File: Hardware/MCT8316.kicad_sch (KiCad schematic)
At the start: 17 parts, among them J5 Screw_Terminal_01x03, U11 PC817

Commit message: Update Sche
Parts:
- removed R31: 10K, IVS_FOOTPRINTS:R_0603, symbol IVS_SYMBOLS:R
- removed U11: PC817, Package_DIP:DIP-4_W7.62mm, symbol Isolator:PC817
- added C22: 1uF, IVS_FOOTPRINTS:C_0603, symbol IVS_SYMBOLS:C
- added J6: Screw_Terminal_01x03, TerminalBlock:TerminalBlock_bornier-3_P5.08mm, symbol Connector:Screw_Terminal_01x03
- added J7, J8: Conn_01x03_Pin, Connector_PinHeader_2.54mm:PinHeader_1x03_P2.54mm_Vertical, symbol IVS_SYMBOLS:Conn_01x03_Pin
- added JP1, JP2: SolderJumper_2_Open, IVS_FOOTPRINTS:SolderJumper-2_P1.3mm_Open_RoundedPad1.0x1.5mm, symbol IVS_SYMBOLS:SolderJumper_2_Open
- added L2: 47uH, Inductor_SMD:L_1812_4532Metric, symbol Device:L
- added R32: 330R, IVS_FOOTPRINTS:R_0603, symbol IVS_SYMBOLS:R
- added R33: 1K, IVS_FOOTPRINTS:R_0603, symbol IVS_SYMBOLS:R
- added U12: ISO7721DR, IVS_FOOTPRINTS:SOIC-8, symbol IVS_SYMBOLS:ISO7721DR
- added U13, U14, U15: EL817, Package_DIP:DIP-4_W7.62mm, symbol IVS_SYMBOLS:EL817
- J5: footprint (none) -> TerminalBlock:TerminalBlock_bornier-3_P5.08mm
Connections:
- net +5V_CS: now also U12.8 (VCC2)
- net AVDD: now also J8.3 (Pin_3)
- net GNDD: now also U12.5 (GND2), U13.2, U14.2, U15.2
- net MCT_DIR: now also U15.1
- net MCT_FAULT: now also U13.1
- net MCT_FG: now also R32.2
- net MCT_SCL: now also J6.1 (Pin_1), J6.2 (Pin_2), JP1.2 (B), JP2.2 (B)
- net PWM_BLDC: now also U12.6 (OUTB)
- net MCT_DRBOFF: now reaches U10.21 (DRVOFF)
- net BUCK: now reaches U10.3 (FB_BK)
- net BUCK: now also C22.2, J7.3 (Pin_3), L2.2
- net MCT_BRAKE: now reaches U10.35 (BRAKE)
- net MCT_BRAKE: now also U14.1
- net at U10.4 (GND_BK): now also C22.1
- net at U10.5 (SW_BK): now also L2.1
- net at R25.2: now also U12.3 (INB)
- new net: R32.1, U12.7 (INA)
- new net +3V3: J8.1 (Pin_1)
- new net +3V3_MCU: J8.2 (Pin_2)
- new net +5V: J7.1 (Pin_1), R33.1, U12.1 (VCC1)
- new net +5VA: J7.2 (Pin_2)
- new net GND: J6.3 (Pin_3), U12.4 (GND1), U13.3, U14.3, U15.3
- new net MCU_BRAKE: U14.4
- new net MCU_DIR: U15.4
- new net MCU_FAULT: U13.4
- new net MCU_FG: R33.2, U12.2 (OUTA)
- new net MCU_SCL: JP2.1 (A)
- new net MCU_SDA: JP1.1 (A)
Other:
- moved on the sheet: C20, C21, F1

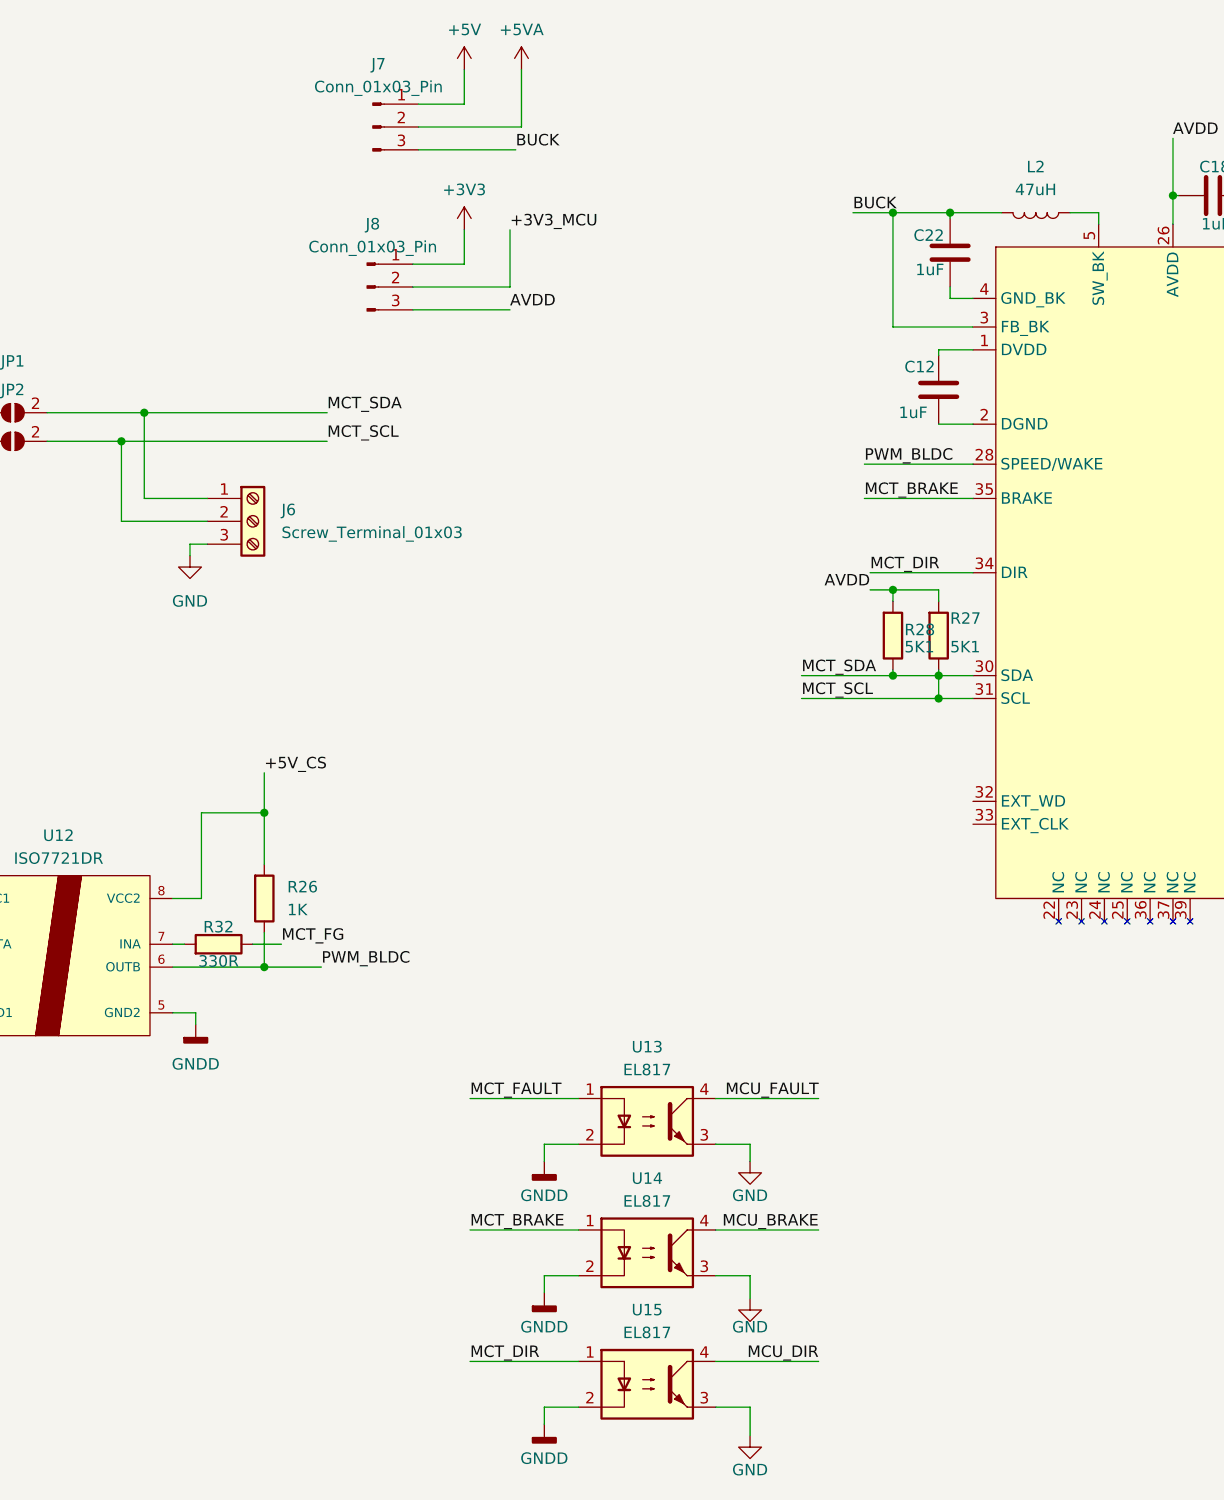
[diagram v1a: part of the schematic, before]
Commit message: Hie BTS, fix GND opto MCT
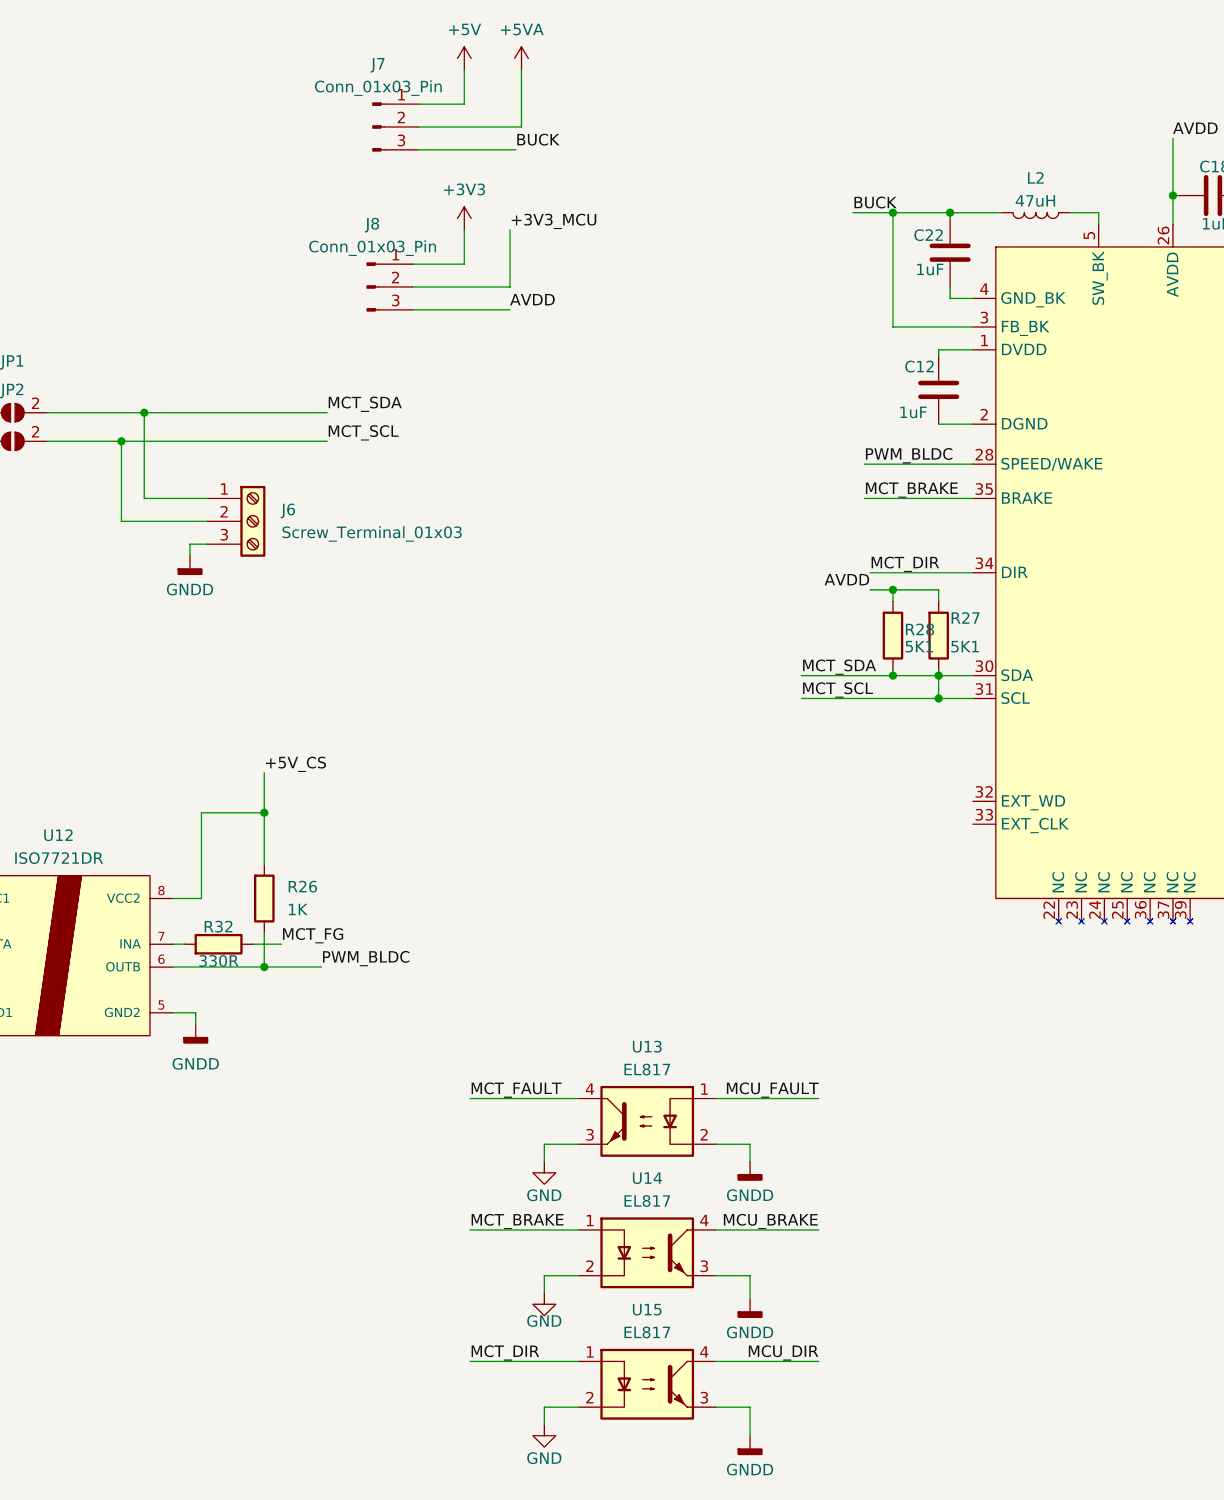
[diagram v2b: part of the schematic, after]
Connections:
- net GND: now also U14.2, U15.2; no longer J6.3 (Pin_3), U14.3, U15.3
- net GNDD: now also J6.3 (Pin_3), U14.3, U15.3; no longer U14.2, U15.2
- net MCT_FAULT: now also U13.4; no longer U13.1
- net MCU_FAULT: now also U13.1; no longer U13.4
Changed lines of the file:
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@@
     (effects (font (size 1.27 1.27)) (justify left bottom))
   )
-  (symbol (lib_id "power:GND") (at 151.13 162.56 0) (unit 1)
-    (in_bom yes) (on_board yes) (dnp no)
-    (property "Reference" "#PWR033" (at 151.13 168.91 0)
-      (effects (font (size 1.27 1.27)) hide)
-    )
-    (property "Value" "GND" (at 151.13 165.735 0)
-      (effects (font (size 1.27 1.27)))
-    )
-    (property "Footprint" "" (at 151.13 162.56 0)
-      (effects (font (size 1.27 1.27)) hide)
-    )
-    (property "Datasheet" "" (at 151.13 162.56 0)
+  (symbol (lib_id "power:GND") (at 128.27 161.925 0) (unit 1)
+    (in_bom yes) (on_board yes) (dnp no)
+    (property "Reference" "#PWR033" (at 128.27 168.275 0)
+      (effects (font (size 1.27 1.27)) hide)
+    )
+    (property "Value" "GND" (at 128.27 165.1 0)
+      (effects (font (size 1.27 1.27)))
+    )
+    (property "Footprint" "" (at 128.27 161.925 0)
+      (effects (font (size 1.27 1.27)) hide)
+    )
+    (property "Datasheet" "" (at 128.27 161.925 0)
       (effects (font (size 1.27 1.27)) hide)
     )
@@
     )
   )
+  (symbol (lib_id "power:GNDD") (at 88.9 80.01 0) (unit 1)
+    (in_bom yes) (on_board yes) (dnp no) (fields_autoplaced)
+    (property "Reference" "#PWR06" (at 88.9 86.36 0)
+      (effects (font (size 1.27 1.27)) hide)
+    )
+    (property "Value" "GNDD" (at 88.9 83.82 0)
+      (effects (font (size 1.27 1.27)))
+    )
+    (property "Footprint" "" (at 88.9 80.01 0)
+      (effects (font (size 1.27 1.27)) hide)
+    )
+    (property "Datasheet" "" (at 88.9 80.01 0)
+      (effects (font (size 1.27 1.27)) hide)
+    )
+    (pin "1")
+    (instances
+      (project "DriverMotor"
+        (path "/8a82bd86-ff43-47ee-a4c0-46ff08914251/719245fa-8c27-4cf8-8d61-6f38548a0446"
+          (reference "#PWR06") (unit 1)
+        )
+      )
+    )
+  )
   (symbol (lib_id "IVS_SYMBOLS:EL817") (at 139.7 157.48 0) (unit 1)
     (in_bom yes) (on_board yes) (dnp no) (fields_autoplaced)
@@
     )
   )
-  (symbol (lib_id "power:GNDD") (at 128.27 147.32 0) (unit 1)
-    (in_bom yes) (on_board yes) (dnp no) (fields_autoplaced)
-    (property "Reference" "#PWR03" (at 128.27 153.67 0)
-      (effects (font (size 1.27 1.27)) hide)
-    )
-    (property "Value" "GNDD" (at 128.27 151.13 0)
-      (effects (font (size 1.27 1.27)))
-    )
-    (property "Footprint" "" (at 128.27 147.32 0)
-      (effects (font (size 1.27 1.27)) hide)
-    )
-    (property "Datasheet" "" (at 128.27 147.32 0)
+  (symbol (lib_id "power:GNDD") (at 151.13 147.32 0) (unit 1)
+    (in_bom yes) (on_board yes) (dnp no) (fields_autoplaced)
+    (property "Reference" "#PWR03" (at 151.13 153.67 0)
+      (effects (font (size 1.27 1.27)) hide)
+    )
+    (property "Value" "GNDD" (at 151.13 151.13 0)
+      (effects (font (size 1.27 1.27)))
+    )
+    (property "Footprint" "" (at 151.13 147.32 0)
+      (effects (font (size 1.27 1.27)) hide)
+    )
+    (property "Datasheet" "" (at 151.13 147.32 0)
       (effects (font (size 1.27 1.27)) hide)
     )
@@
     )
   )
-  (symbol (lib_id "power:GNDD") (at 128.27 176.53 0) (unit 1)
-    (in_bom yes) (on_board yes) (dnp no) (fields_autoplaced)
-    (property "Reference" "#PWR010" (at 128.27 182.88 0)
-      (effects (font (size 1.27 1.27)) hide)
-    )
-    (property "Value" "GNDD" (at 128.27 180.34 0)
-      (effects (font (size 1.27 1.27)))
-    )
-    (property "Footprint" "" (at 128.27 176.53 0)
-      (effects (font (size 1.27 1.27)) hide)
-    )
-    (property "Datasheet" "" (at 128.27 176.53 0)
+  (symbol (lib_id "power:GNDD") (at 151.13 177.8 0) (unit 1)
+    (in_bom yes) (on_board yes) (dnp no)
+    (property "Reference" "#PWR010" (at 151.13 184.15 0)
+      (effects (font (size 1.27 1.27)) hide)
+    )
+    (property "Value" "GNDD" (at 151.13 181.61 0)
+      (effects (font (size 1.27 1.27)))
+    )
+    (property "Footprint" "" (at 151.13 177.8 0)
+      (effects (font (size 1.27 1.27)) hide)
+    )
+    (property "Datasheet" "" (at 151.13 177.8 0)
       (effects (font (size 1.27 1.27)) hide)
     )
@@
   (symbol (lib_id "Device:L") (at 182.88 41.91 270) (unit 1)
     (in_bom yes) (on_board yes) (dnp no) (fields_autoplaced)
-    (property "Reference" "L2" (at 182.88 36.83 90)
-      (effects (font (size 1.27 1.27)))
-    )
-    (property "Value" "47uH" (at 182.88 39.37 90)
+    (property "Reference" "L2" (at 182.88 38.1 90)
+      (effects (font (size 1.27 1.27)))
+    )
+    (property "Value" "47uH" (at 182.88 40.64 90)
       (effects (font (size 1.27 1.27)))
     )
@@
     )
   )
-  (symbol (lib_id "power:GND") (at 151.13 177.8 0) (unit 1)
-    (in_bom yes) (on_board yes) (dnp no)
-    (property "Reference" "#PWR048" (at 151.13 184.15 0)
-      (effects (font (size 1.27 1.27)) hide)
-    )
-    (property "Value" "GND" (at 151.13 181.61 0)
-      (effects (font (size 1.27 1.27)))
-    )
-    (property "Footprint" "" (at 151.13 177.8 0)
-      (effects (font (size 1.27 1.27)) hide)
-    )
-    (property "Datasheet" "" (at 151.13 177.8 0)
+  (symbol (lib_id "power:GND") (at 128.27 176.53 0) (unit 1)
+    (in_bom yes) (on_board yes) (dnp no)
+    (property "Reference" "#PWR048" (at 128.27 182.88 0)
+      (effects (font (size 1.27 1.27)) hide)
+    )
+    (property "Value" "GND" (at 128.27 180.34 0)
+      (effects (font (size 1.27 1.27)))
+    )
+    (property "Footprint" "" (at 128.27 176.53 0)
+      (effects (font (size 1.27 1.27)) hide)
+    )
+    (property "Datasheet" "" (at 128.27 176.53 0)
       (effects (font (size 1.27 1.27)) hide)
     )
@@
     )
   )
-  (symbol (lib_id "power:GND") (at 88.9 80.01 0) (unit 1)
-    (in_bom yes) (on_board yes) (dnp no) (fields_autoplaced)
-    (property "Reference" "#PWR031" (at 88.9 86.36 0)
-      (effects (font (size 1.27 1.27)) hide)
-    )
-    (property "Value" "GND" (at 88.9 85.09 0)
-      (effects (font (size 1.27 1.27)))
-    )
-    (property "Footprint" "" (at 88.9 80.01 0)
-      (effects (font (size 1.27 1.27)) hide)
-    )
-    (property "Datasheet" "" (at 88.9 80.01 0)
-      (effects (font (size 1.27 1.27)) hide)
-    )
-    (pin "1")
-    (instances
-      (project "DriverMotor"
-        (path "/8a82bd86-ff43-47ee-a4c0-46ff08914251/719245fa-8c27-4cf8-8d61-6f38548a0446"
-          (reference "#PWR031") (unit 1)
-        )
-      )
-    )
-  )
   (symbol (lib_id "IVS_SYMBOLS:Conn_01x03_Pin") (at 108.585 50.165 0) (unit 1)
     (in_bom yes) (on_board yes) (dnp no) (fields_autoplaced)
@@
     )
   )
-  (symbol (lib_id "power:GNDD") (at 128.27 161.925 0) (unit 1)
-    (in_bom yes) (on_board yes) (dnp no) (fields_autoplaced)
-    (property "Reference" "#PWR08" (at 128.27 168.275 0)
-      (effects (font (size 1.27 1.27)) hide)
-    )
-    (property "Value" "GNDD" (at 128.27 165.735 0)
-      (effects (font (size 1.27 1.27)))
-    )
-    (property "Footprint" "" (at 128.27 161.925 0)
-      (effects (font (size 1.27 1.27)) hide)
-    )
-    (property "Datasheet" "" (at 128.27 161.925 0)
+  (symbol (lib_id "power:GNDD") (at 151.13 162.56 0) (unit 1)
+    (in_bom yes) (on_board yes) (dnp no)
+    (property "Reference" "#PWR08" (at 151.13 168.91 0)
+      (effects (font (size 1.27 1.27)) hide)
+    )
+    (property "Value" "GNDD" (at 151.13 166.37 0)
+      (effects (font (size 1.27 1.27)))
+    )
+    (property "Footprint" "" (at 151.13 162.56 0)
+      (effects (font (size 1.27 1.27)) hide)
+    )
+    (property "Datasheet" "" (at 151.13 162.56 0)
       (effects (font (size 1.27 1.27)) hide)
     )
@@
     )
   )
-  (symbol (lib_id "power:GND") (at 151.13 147.32 0) (unit 1)
-    (in_bom yes) (on_board yes) (dnp no)
-    (property "Reference" "#PWR015" (at 151.13 153.67 0)
-      (effects (font (size 1.27 1.27)) hide)
-    )
-    (property "Value" "GND" (at 151.13 151.13 0)
-      (effects (font (size 1.27 1.27)))
-    )
-    (property "Footprint" "" (at 151.13 147.32 0)
-      (effects (font (size 1.27 1.27)) hide)
-    )
-    (property "Datasheet" "" (at 151.13 147.32 0)
+  (symbol (lib_id "power:GND") (at 128.27 147.32 0) (unit 1)
+    (in_bom yes) (on_board yes) (dnp no)
+    (property "Reference" "#PWR015" (at 128.27 153.67 0)
+      (effects (font (size 1.27 1.27)) hide)
+    )
+    (property "Value" "GND" (at 128.27 151.13 0)
+      (effects (font (size 1.27 1.27)))
+    )
+    (property "Footprint" "" (at 128.27 147.32 0)
+      (effects (font (size 1.27 1.27)) hide)
+    )
+    (property "Datasheet" "" (at 128.27 147.32 0)
       (effects (font (size 1.27 1.27)) hide)
     )
@@
     )
   )
-  (symbol (lib_id "IVS_SYMBOLS:EL817") (at 139.7 142.875 0) (unit 1)
-    (in_bom yes) (on_board yes) (dnp no) (fields_autoplaced)
+  (symbol (lib_id "IVS_SYMBOLS:EL817") (at 139.7 142.875 0) (mirror y) (unit 1)
+    (in_bom yes) (on_board yes) (dnp no)
     (property "Reference" "U13" (at 139.7 134.62 0)
       (effects (font (size 1.27 1.27)))
@@
       (effects (font (size 1.27 1.27)))
     )
-    (property "Footprint" "Package_DIP:DIP-4_W7.62mm" (at 134.62 147.955 0)
+    (property "Footprint" "Package_DIP:DIP-4_W7.62mm" (at 144.78 147.955 0)
       (effects (font (size 1.27 1.27) italic) (justify left) hide)
     )

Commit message: Up schematic
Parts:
- removed U10: ~, symbol IVS_SYMBOLS:MxT-F8316
- added J12: Screw_Terminal_01x04, Connector_PinHeader_2.54mm:PinHeader_1x04_P2.54mm_Vertical, symbol Connector:Screw_Terminal_01x04
- added R35: 1K, IVS_FOOTPRINTS:R_0603, symbol IVS_SYMBOLS:R
- added U10: MCT8316, IVS_FOOTPRINTS:VQFN-40-1EP_7x7mm_P0.5mm_EP5.7x3.7mm_ThermalVias, symbol IVS_SYMBOLS:MCT8316
- C21: footprint Capacitor_THT:CP_Radial_D4.0mm_P2.00mm -> IVS_FOOTPRINTS:CP-Tantalum-EIA-3528-15-AVX-H
- J6: footprint TerminalBlock:TerminalBlock_bornier-3_P5.08mm -> Connector_PinHeader_2.54mm:PinHeader_1x03_P2.54mm_Vertical
- U13, U14, U15: footprint Package_DIP:DIP-4_W7.62mm -> IVS_FOOTPRINTS:OptoIsolation-EL357N-G
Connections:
- net +5V_CS: now also R35.1
- net AVDD: now also U10.26 (AVDD)
- net BUCK: now also L2.1, U10.3 (FB_BK); no longer L2.2
- net GND: now also J12.2 (Pin_2)
- net GNDD: now also U10.12 (PGND), U10.15 (PGND), U10.18 (PGND), U10.27 (AGND)
- net MA: now also U10.13 (OUTA), U10.14 (OUTA)
- net MB: now also U10.16 (OUTB), U10.17 (OUTB)
- net MC: now also U10.19 (OUTC), U10.20 (OUTC)
- net MCT_BRAKE: now also U14.4, U10.35 (BRAKE); no longer U14.1
- net MCT_DIR: now also U15.4, U10.34 (DIR); no longer U15.1
- net MCT_FAULT: now also U13.1, U10.40 (nFAULT); no longer U13.4
- net MCT_FG: now also U10.29 (FG)
- net MCT_SCL: now also U10.30 (SDA), U10.31 (SCL)
- net MCT_SOX: now also U10.36 (DACOUT2/SOX)
- net MCU_BRAKE: now also U14.1, J12.4 (Pin_4); no longer U14.4
- net MCU_DIR: now also U15.1, J12.3 (Pin_3); no longer U15.4
- net MCU_FAULT: now also U13.4; no longer U13.1
- net MCU_PWM_BLDC: now also J12.1 (Pin_1)
- net PWM_BLDC: now also U10.28 (SPEED/WAKE)
- net at C12.1: now also U10.1 (DVDD)
- net at C19.2, C20.2, C21.1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: now also U10.10 (VM), U10.11 (VM), U10.9 (VM)
- net at C12.2: now also U10.2 (DGND)
- net at C22.1: now also U10.4 (GND_BK)
- net at C13.1: now also U10.6 (CPL)
- net at C13.2: now also U10.7 (CPH)
- net at C19.1: now also U10.8 (CP)
- new net: R35.2, U10.21 (DRVOFF)
- new net: L2.2, U10.5 (SW_BK)
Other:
- moved on the sheet: L2
